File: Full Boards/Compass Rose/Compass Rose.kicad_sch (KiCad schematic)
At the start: 245 parts, among them J1 Program Header, J2 Future Bonding, Q10 2N3904, Q11 AO3401A, Q12 2N3904, Q7 AO3401A, Q8 2N3904, Q9 AO3401A, SW1 SW_MEC_5G, SW2 SW_MEC_5G, U1 ISO1044BD, U2 LM1117MP-5.0, U3 MAX3232, U4 STM32C092KCT6, U5 IS31FL3731-SA, U6 FM24CL64B-G, U7 FM24CL64B-G

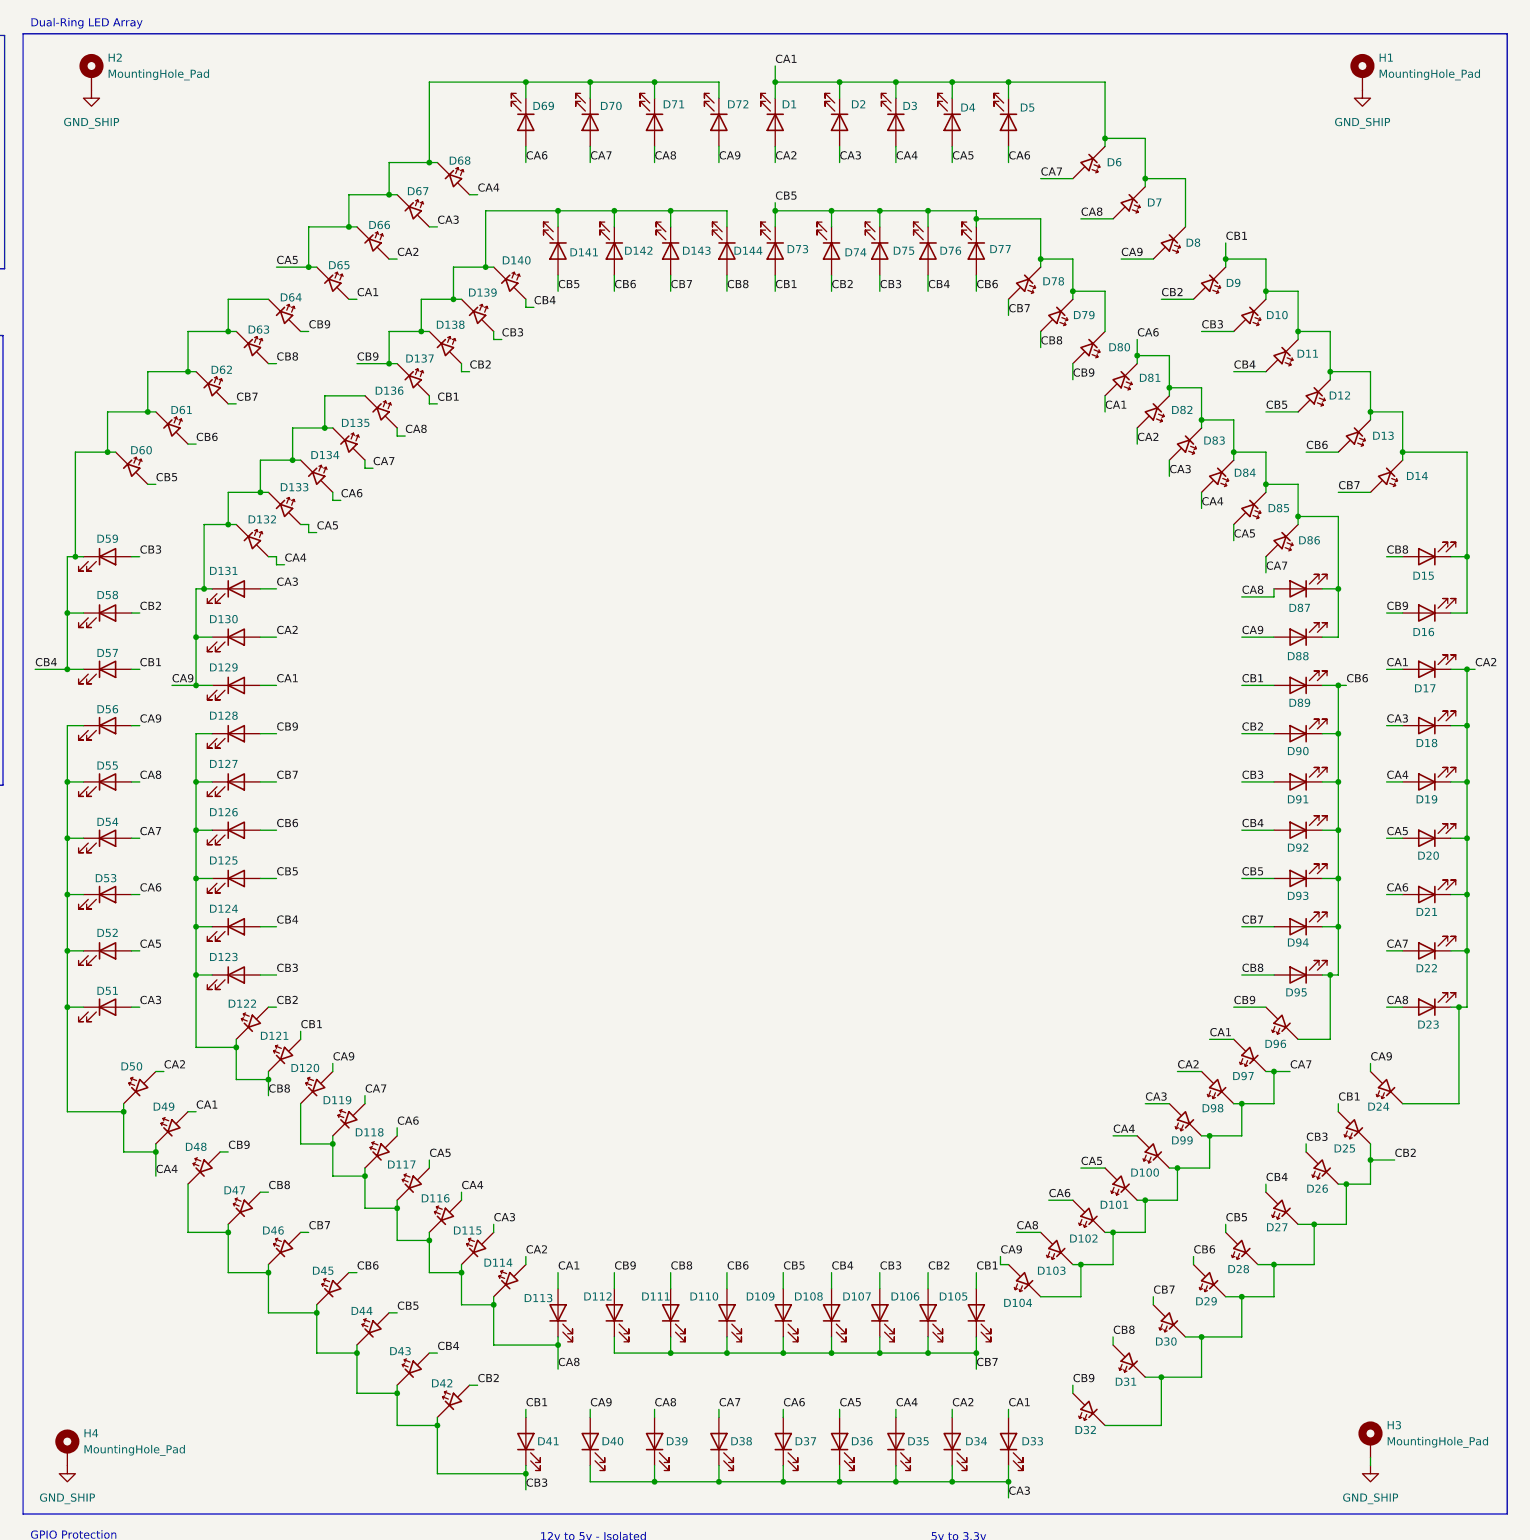
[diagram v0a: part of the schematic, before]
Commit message: Started updating the compass rose.
Signed-off-by: digimer <digital.mermaid@gmail.com>
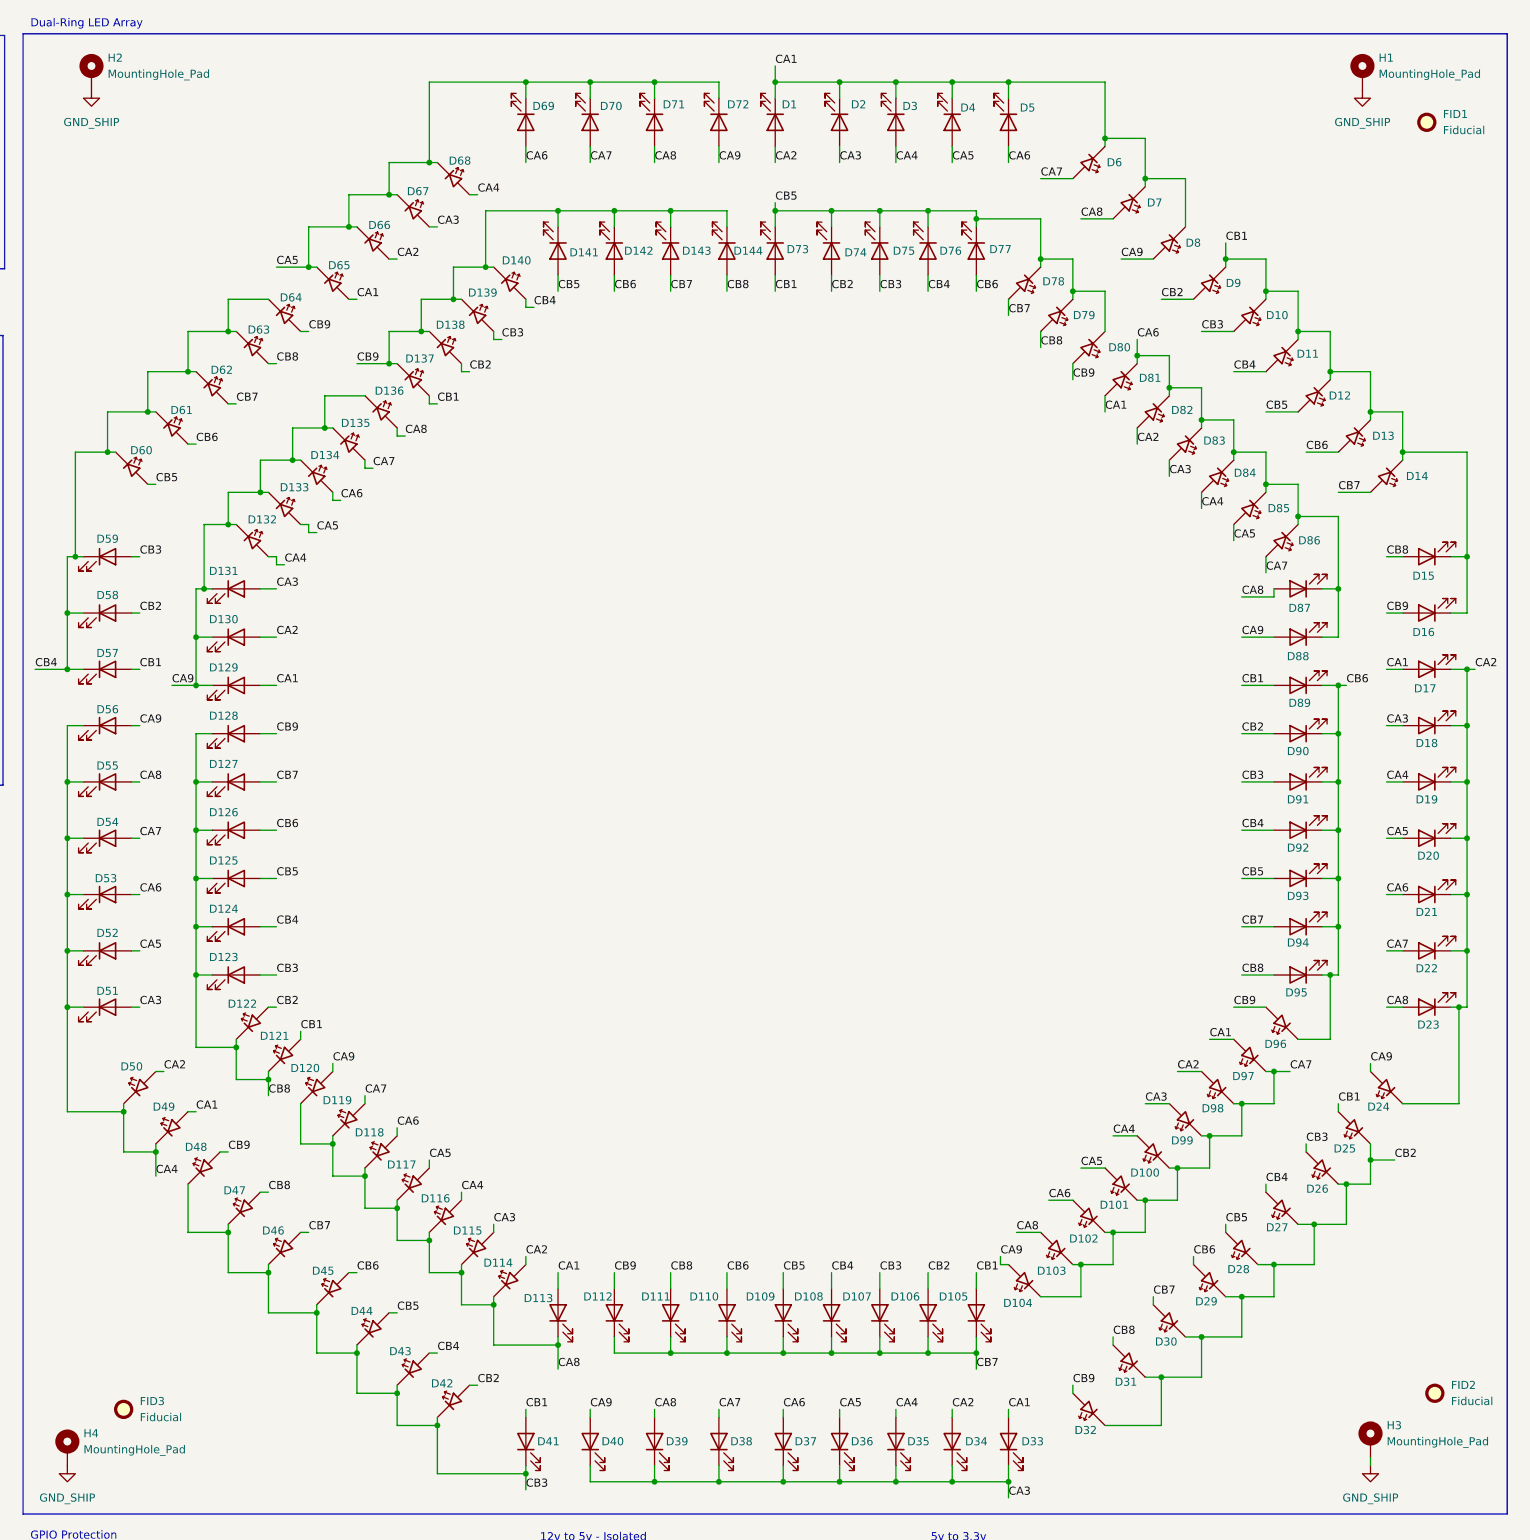
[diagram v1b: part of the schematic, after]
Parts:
- added FID1, FID2, FID3: Fiducial, symbol Mechanical:Fiducial
- DE1, DE2, LCD1, N2K1: value ~ -> (none)

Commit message: First update of the Compass Rose PCB.
Signed-off-by: digimer <digital.mermaid@gmail.com>
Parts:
- removed C6: TDK FA28NP01H152JNU06, mr-stuff:TDK CAPRB500W50L400T250H550, symbol mr-parts:TDK FA28NP01H152JNU06
- removed J2: Future Bonding, Connector_PinHeader_2.54mm:PinHeader_1x03_P2.54mm_Vertical, symbol Connector:Conn_01x03_Pin
- removed LR1: NCV8730ASN500T1G, mr-stuff:TSOP-5_483_OSI, symbol mr-parts:NCV8730ASN500T1G
- removed N2K1: (no value), mr-stuff:M12B-05PMMR, symbol mr-parts:M12B-05PMMR
- removed PS2: SPBW06F-05, mr-stuff:SPBW06F05, symbol mr-parts:SPBW06F-05
- removed SW1, SW2: SW_MEC_5G, mr-stuff:SW_TS03-66-50-BK-160-LCR-D-67, symbol Switch:SW_MEC_5G
- removed TP1: TP_VRAW, Connector_PinHeader_2.54mm:PinHeader_1x01_P2.54mm_Vertical, symbol Connector:Conn_01x01_Pin
- removed TP2, TP6: GND_SHIP, Connector_PinHeader_2.54mm:PinHeader_1x01_P2.54mm_Vertical, symbol Connector:Conn_01x01_Pin
- removed TP5: +5V_SHIP, Connector_PinHeader_2.54mm:PinHeader_1x01_P2.54mm_Vertical, symbol Connector:Conn_01x01_Pin
- removed U3: MAX3232, Package_SO:TSSOP-16_4.4x5mm_P0.65mm, symbol mr-parts:TI MAX3232EIPWRQ1
- added C6: 1500 pF, mr-stuff:TDK FA 5.0mm, symbol Device:C
- added IDCB1: SPBW06F-05, mr-stuff:Meanwell SPBW06F05, symbol mr-parts:Meanwell SPBW06F-05
- added J2: Opional Bond, Connector_PinHeader_2.54mm:PinHeader_1x02_P2.54mm_Vertical, symbol Connector:Conn_01x02_Pin
- added LVR1: NCV8730ASN500T1G, mr-stuff:Onsemi NCV8730, symbol mr-parts:Onsemi NCV8730ASN500T1G
- added RST1: MAX3232, mr-stuff:TI MAX3232EIPWRQ1, symbol mr-parts:TI MAX3232EIPWRQ1
- added SW1: Boot, mr-stuff:Same Sky TS03-66, symbol mr-parts:Same Sky TS03-66-50-BK-160-LCR-D-67
- added SW2: Reset, mr-stuff:Same Sky TS03-66, symbol mr-parts:Same Sky TS03-66-50-BK-160-LCR-D-67
- added TB1: 1862440, mr-stuff:Phoenix Contact 1862440, symbol mr-parts:Phoenix Contact 1862440
- added TP1: Iso Power, Connector_PinHeader_2.54mm:PinHeader_1x01_P2.54mm_Vertical, symbol Connector:Conn_01x02_Pin
- C14: footprint mr-stuff:RCER71E475K2A2H03B -> mr-stuff:Murata RCER71E
- D1: renamed from D145; Part (none) -> STM 1N5822RL
- DE1: value (none) -> L77SDE09SA4CH4F; symbol mr-parts:DE9_Socket -> mr-parts:Amphenol L77SDE09SA4CH4F; Part (none) -> Amphenol L77SDE09SA4CH4F
- ICT1: renamed from U1; value ISO1044BD -> TI_ISO1044BDR; symbol Interface_CAN_LIN:ISO1044BD -> mr-parts:TI_ISO1044BDR; Part (none) -> TI ISO1044BDR
- LCD1: value (none) -> 2x16 Char RGB I2C; footprint mr-stuff:NHD-0216K3Z-NS(RGB)-FBW-V3 -> mr-stuff:Newhaven Display NHD-0216K3Z-NS(RGB)-FBW-V3; symbol mr-parts:NHD-0216K3Z-FS(RGB)-FBW-V3 -> mr-parts:Newhaven Display NHD-0216K3Z-FS(RGB)-FBW-V3
- LED1: renamed from D1; value LED -> WP383SURDTK; footprint mr-stuff:WP383SURDTK -> mr-stuff:Kingbright WP383SURDTK; symbol Device:LED -> mr-parts:Kingbright WP383SURDTK; Part (none) -> Kingbright WP383SURDTK
- LED10: renamed from D10; value LED_45deg -> WP383SURDTK; footprint mr-stuff:WP383SURDTK -> mr-stuff:Kingbright WP383SURDTK; symbol Device:LED_45deg -> mr-parts:Kingbright_WP383SURDTK_45DEG; Part (none) -> Kingbright WP383SURDTK
- LED100: renamed from D100; value LED_45deg -> WP383SURDTK; footprint mr-stuff:WP383SURDTK -> mr-stuff:Kingbright WP383SURDTK; symbol Device:LED_45deg -> mr-parts:Kingbright_WP383SURDTK_45DEG; Part (none) -> Kingbright WP383SURDTK
- LED101: renamed from D101; value LED_45deg -> WP383SURDTK; footprint mr-stuff:WP383SURDTK -> mr-stuff:Kingbright WP383SURDTK; symbol Device:LED_45deg -> mr-parts:Kingbright_WP383SURDTK_45DEG; Part (none) -> Kingbright WP383SURDTK
- LED102: renamed from D102; value LED_45deg -> WP383SURDTK; footprint mr-stuff:WP383SURDTK -> mr-stuff:Kingbright WP383SURDTK; symbol Device:LED_45deg -> mr-parts:Kingbright_WP383SURDTK_45DEG; Part (none) -> Kingbright WP383SURDTK
- LED103: renamed from D103; value LED_45deg -> WP383SURDTK; footprint mr-stuff:WP383SURDTK -> mr-stuff:Kingbright WP383SURDTK; symbol Device:LED_45deg -> mr-parts:Kingbright_WP383SURDTK_45DEG; Part (none) -> Kingbright WP383SURDTK
- LED104: renamed from D104; value LED_45deg -> WP383SURDTK; footprint mr-stuff:WP383SURDTK -> mr-stuff:Kingbright WP383SURDTK; symbol Device:LED_45deg -> mr-parts:Kingbright_WP383SURDTK_45DEG; Part (none) -> Kingbright WP383SURDTK
- LED105: renamed from D105; value LED -> WP383SURDTK; footprint mr-stuff:WP383SURDTK -> mr-stuff:Kingbright WP383SURDTK; symbol Device:LED -> mr-parts:Kingbright WP383SURDTK; Part (none) -> Kingbright WP383SURDTK
- LED106: renamed from D106; value LED -> WP383SURDTK; footprint mr-stuff:WP383SURDTK -> mr-stuff:Kingbright WP383SURDTK; symbol Device:LED -> mr-parts:Kingbright WP383SURDTK; Part (none) -> Kingbright WP383SURDTK
- LED107: renamed from D107; value LED -> WP383SURDTK; footprint mr-stuff:WP383SURDTK -> mr-stuff:Kingbright WP383SURDTK; symbol Device:LED -> mr-parts:Kingbright WP383SURDTK; Part (none) -> Kingbright WP383SURDTK
- LED108: renamed from D108; value LED -> WP383SURDTK; footprint mr-stuff:WP383SURDTK -> mr-stuff:Kingbright WP383SURDTK; symbol Device:LED -> mr-parts:Kingbright WP383SURDTK; Part (none) -> Kingbright WP383SURDTK
- LED109: renamed from D109; value LED -> WP383SURDTK; footprint mr-stuff:WP383SURDTK -> mr-stuff:Kingbright WP383SURDTK; symbol Device:LED -> mr-parts:Kingbright WP383SURDTK; Part (none) -> Kingbright WP383SURDTK
- LED11: renamed from D11; value LED_45deg -> WP383SURDTK; footprint mr-stuff:WP383SURDTK -> mr-stuff:Kingbright WP383SURDTK; symbol Device:LED_45deg -> mr-parts:Kingbright_WP383SURDTK_45DEG; Part (none) -> Kingbright WP383SURDTK
- LED110: renamed from D110; value LED -> WP383SURDTK; footprint mr-stuff:WP383SURDTK -> mr-stuff:Kingbright WP383SURDTK; symbol Device:LED -> mr-parts:Kingbright WP383SURDTK; Part (none) -> Kingbright WP383SURDTK
- LED111: renamed from D111; value LED -> WP383SURDTK; footprint mr-stuff:WP383SURDTK -> mr-stuff:Kingbright WP383SURDTK; symbol Device:LED -> mr-parts:Kingbright WP383SURDTK; Part (none) -> Kingbright WP383SURDTK
- LED112: renamed from D112; value LED -> WP383SURDTK; footprint mr-stuff:WP383SURDTK -> mr-stuff:Kingbright WP383SURDTK; symbol Device:LED -> mr-parts:Kingbright WP383SURDTK; Part (none) -> Kingbright WP383SURDTK
- LED113: renamed from D113; value LED -> WP383SURDTK; footprint mr-stuff:WP383SURDTK -> mr-stuff:Kingbright WP383SURDTK; symbol Device:LED -> mr-parts:Kingbright WP383SURDTK; Part (none) -> Kingbright WP383SURDTK
- LED114: renamed from D114; value LED_45deg -> WP383SURDTK; footprint mr-stuff:WP383SURDTK -> mr-stuff:Kingbright WP383SURDTK; symbol Device:LED_45deg -> mr-parts:Kingbright_WP383SURDTK_45DEG; Part (none) -> Kingbright WP383SURDTK
- LED115: renamed from D115; value LED_45deg -> WP383SURDTK; footprint mr-stuff:WP383SURDTK -> mr-stuff:Kingbright WP383SURDTK; symbol Device:LED_45deg -> mr-parts:Kingbright_WP383SURDTK_45DEG; Part (none) -> Kingbright WP383SURDTK
- LED116: renamed from D116; value LED_45deg -> WP383SURDTK; footprint mr-stuff:WP383SURDTK -> mr-stuff:Kingbright WP383SURDTK; symbol Device:LED_45deg -> mr-parts:Kingbright_WP383SURDTK_45DEG; Part (none) -> Kingbright WP383SURDTK
- LED117: renamed from D117; value LED_45deg -> WP383SURDTK; footprint mr-stuff:WP383SURDTK -> mr-stuff:Kingbright WP383SURDTK; symbol Device:LED_45deg -> mr-parts:Kingbright_WP383SURDTK_45DEG; Part (none) -> Kingbright WP383SURDTK
- LED118: renamed from D118; value LED_45deg -> WP383SURDTK; footprint mr-stuff:WP383SURDTK -> mr-stuff:Kingbright WP383SURDTK; symbol Device:LED_45deg -> mr-parts:Kingbright_WP383SURDTK_45DEG; Part (none) -> Kingbright WP383SURDTK
- LED119: renamed from D119; value LED_45deg -> WP383SURDTK; footprint mr-stuff:WP383SURDTK -> mr-stuff:Kingbright WP383SURDTK; symbol Device:LED_45deg -> mr-parts:Kingbright_WP383SURDTK_45DEG; Part (none) -> Kingbright WP383SURDTK
- LED12: renamed from D12; value LED_45deg -> WP383SURDTK; footprint mr-stuff:WP383SURDTK -> mr-stuff:Kingbright WP383SURDTK; symbol Device:LED_45deg -> mr-parts:Kingbright_WP383SURDTK_45DEG; Part (none) -> Kingbright WP383SURDTK
- LED120: renamed from D120; value LED_45deg -> WP383SURDTK; footprint mr-stuff:WP383SURDTK -> mr-stuff:Kingbright WP383SURDTK; symbol Device:LED_45deg -> mr-parts:Kingbright_WP383SURDTK_45DEG; Part (none) -> Kingbright WP383SURDTK
- LED121: renamed from D121; value LED_45deg -> WP383SURDTK; footprint mr-stuff:WP383SURDTK -> mr-stuff:Kingbright WP383SURDTK; symbol Device:LED_45deg -> mr-parts:Kingbright_WP383SURDTK_45DEG; Part (none) -> Kingbright WP383SURDTK
- LED122: renamed from D122; value LED_45deg -> WP383SURDTK; footprint mr-stuff:WP383SURDTK -> mr-stuff:Kingbright WP383SURDTK; symbol Device:LED_45deg -> mr-parts:Kingbright_WP383SURDTK_45DEG; Part (none) -> Kingbright WP383SURDTK
- LED123: renamed from D123; value LED -> WP383SURDTK; footprint mr-stuff:WP383SURDTK -> mr-stuff:Kingbright WP383SURDTK; symbol Device:LED -> mr-parts:Kingbright WP383SURDTK; Part (none) -> Kingbright WP383SURDTK
- LED124: renamed from D124; value LED -> WP383SURDTK; footprint mr-stuff:WP383SURDTK -> mr-stuff:Kingbright WP383SURDTK; symbol Device:LED -> mr-parts:Kingbright WP383SURDTK; Part (none) -> Kingbright WP383SURDTK
- LED125: renamed from D125; value LED -> WP383SURDTK; footprint mr-stuff:WP383SURDTK -> mr-stuff:Kingbright WP383SURDTK; symbol Device:LED -> mr-parts:Kingbright WP383SURDTK; Part (none) -> Kingbright WP383SURDTK
- LED126: renamed from D126; value LED -> WP383SURDTK; footprint mr-stuff:WP383SURDTK -> mr-stuff:Kingbright WP383SURDTK; symbol Device:LED -> mr-parts:Kingbright WP383SURDTK; Part (none) -> Kingbright WP383SURDTK
- LED127: renamed from D127; value LED -> WP383SURDTK; footprint mr-stuff:WP383SURDTK -> mr-stuff:Kingbright WP383SURDTK; symbol Device:LED -> mr-parts:Kingbright WP383SURDTK; Part (none) -> Kingbright WP383SURDTK
- LED128: renamed from D128; value LED -> WP383SURDTK; footprint mr-stuff:WP383SURDTK -> mr-stuff:Kingbright WP383SURDTK; symbol Device:LED -> mr-parts:Kingbright WP383SURDTK; Part (none) -> Kingbright WP383SURDTK
- LED129: renamed from D129; value LED -> WP383SURDTK; footprint mr-stuff:WP383SURDTK -> mr-stuff:Kingbright WP383SURDTK; symbol Device:LED -> mr-parts:Kingbright WP383SURDTK; Part (none) -> Kingbright WP383SURDTK
- LED13: renamed from D13; value LED_45deg -> WP383SURDTK; footprint mr-stuff:WP383SURDTK -> mr-stuff:Kingbright WP383SURDTK; symbol Device:LED_45deg -> mr-parts:Kingbright_WP383SURDTK_45DEG; Part (none) -> Kingbright WP383SURDTK
- LED130: renamed from D130; value LED -> WP383SURDTK; footprint mr-stuff:WP383SURDTK -> mr-stuff:Kingbright WP383SURDTK; symbol Device:LED -> mr-parts:Kingbright WP383SURDTK; Part (none) -> Kingbright WP383SURDTK
- LED131: renamed from D131; value LED -> WP383SURDTK; footprint mr-stuff:WP383SURDTK -> mr-stuff:Kingbright WP383SURDTK; symbol Device:LED -> mr-parts:Kingbright WP383SURDTK; Part (none) -> Kingbright WP383SURDTK
- LED132: renamed from D132; value LED_45deg -> WP383SURDTK; footprint mr-stuff:WP383SURDTK -> mr-stuff:Kingbright WP383SURDTK; symbol Device:LED_45deg -> mr-parts:Kingbright_WP383SURDTK_45DEG; Part (none) -> Kingbright WP383SURDTK
- LED133: renamed from D133; value LED_45deg -> WP383SURDTK; footprint mr-stuff:WP383SURDTK -> mr-stuff:Kingbright WP383SURDTK; symbol Device:LED_45deg -> mr-parts:Kingbright_WP383SURDTK_45DEG; Part (none) -> Kingbright WP383SURDTK
- LED134: renamed from D134; value LED_45deg -> WP383SURDTK; footprint mr-stuff:WP383SURDTK -> mr-stuff:Kingbright WP383SURDTK; symbol Device:LED_45deg -> mr-parts:Kingbright_WP383SURDTK_45DEG; Part (none) -> Kingbright WP383SURDTK
- LED135: renamed from D135; value LED_45deg -> WP383SURDTK; footprint mr-stuff:WP383SURDTK -> mr-stuff:Kingbright WP383SURDTK; symbol Device:LED_45deg -> mr-parts:Kingbright_WP383SURDTK_45DEG; Part (none) -> Kingbright WP383SURDTK
- LED136: renamed from D136; value LED_45deg -> WP383SURDTK; footprint mr-stuff:WP383SURDTK -> mr-stuff:Kingbright WP383SURDTK; symbol Device:LED_45deg -> mr-parts:Kingbright_WP383SURDTK_45DEG; Part (none) -> Kingbright WP383SURDTK
- LED137: renamed from D137; value LED_45deg -> WP383SURDTK; footprint mr-stuff:WP383SURDTK -> mr-stuff:Kingbright WP383SURDTK; symbol Device:LED_45deg -> mr-parts:Kingbright_WP383SURDTK_45DEG; Part (none) -> Kingbright WP383SURDTK
- LED138: renamed from D138; value LED_45deg -> WP383SURDTK; footprint mr-stuff:WP383SURDTK -> mr-stuff:Kingbright WP383SURDTK; symbol Device:LED_45deg -> mr-parts:Kingbright_WP383SURDTK_45DEG; Part (none) -> Kingbright WP383SURDTK
- LED139: renamed from D139; value LED_45deg -> WP383SURDTK; footprint mr-stuff:WP383SURDTK -> mr-stuff:Kingbright WP383SURDTK; symbol Device:LED_45deg -> mr-parts:Kingbright_WP383SURDTK_45DEG; Part (none) -> Kingbright WP383SURDTK
- LED14: renamed from D14; value LED_45deg -> WP383SURDTK; footprint mr-stuff:WP383SURDTK -> mr-stuff:Kingbright WP383SURDTK; symbol Device:LED_45deg -> mr-parts:Kingbright_WP383SURDTK_45DEG; Part (none) -> Kingbright WP383SURDTK
- LED140: renamed from D140; value LED_45deg -> WP383SURDTK; footprint mr-stuff:WP383SURDTK -> mr-stuff:Kingbright WP383SURDTK; symbol Device:LED_45deg -> mr-parts:Kingbright_WP383SURDTK_45DEG; Part (none) -> Kingbright WP383SURDTK
- LED141: renamed from D141; value LED -> WP383SURDTK; footprint mr-stuff:WP383SURDTK -> mr-stuff:Kingbright WP383SURDTK; symbol Device:LED -> mr-parts:Kingbright WP383SURDTK; Part (none) -> Kingbright WP383SURDTK
- LED142: renamed from D142; value LED -> WP383SURDTK; footprint mr-stuff:WP383SURDTK -> mr-stuff:Kingbright WP383SURDTK; symbol Device:LED -> mr-parts:Kingbright WP383SURDTK; Part (none) -> Kingbright WP383SURDTK
- LED143: renamed from D143; value LED -> WP383SURDTK; footprint mr-stuff:WP383SURDTK -> mr-stuff:Kingbright WP383SURDTK; symbol Device:LED -> mr-parts:Kingbright WP383SURDTK; Part (none) -> Kingbright WP383SURDTK
- LED144: renamed from D144; value LED -> WP383SURDTK; footprint mr-stuff:WP383SURDTK -> mr-stuff:Kingbright WP383SURDTK; symbol Device:LED -> mr-parts:Kingbright WP383SURDTK; Part (none) -> Kingbright WP383SURDTK
- LED15: renamed from D15; value LED -> WP383SURDTK; footprint mr-stuff:WP383SURDTK -> mr-stuff:Kingbright WP383SURDTK; symbol Device:LED -> mr-parts:Kingbright WP383SURDTK; Part (none) -> Kingbright WP383SURDTK
- LED16: renamed from D16; value LED -> WP383SURDTK; footprint mr-stuff:WP383SURDTK -> mr-stuff:Kingbright WP383SURDTK; symbol Device:LED -> mr-parts:Kingbright WP383SURDTK; Part (none) -> Kingbright WP383SURDTK
- LED17: renamed from D17; value LED -> WP383SURDTK; footprint mr-stuff:WP383SURDTK -> mr-stuff:Kingbright WP383SURDTK; symbol Device:LED -> mr-parts:Kingbright WP383SURDTK; Part (none) -> Kingbright WP383SURDTK
- LED18: renamed from D18; value LED -> WP383SURDTK; footprint mr-stuff:WP383SURDTK -> mr-stuff:Kingbright WP383SURDTK; symbol Device:LED -> mr-parts:Kingbright WP383SURDTK; Part (none) -> Kingbright WP383SURDTK
- LED19: renamed from D19; value LED -> WP383SURDTK; footprint mr-stuff:WP383SURDTK -> mr-stuff:Kingbright WP383SURDTK; symbol Device:LED -> mr-parts:Kingbright WP383SURDTK; Part (none) -> Kingbright WP383SURDTK
- LED2: renamed from D2; value LED -> WP383SURDTK; footprint mr-stuff:WP383SURDTK -> mr-stuff:Kingbright WP383SURDTK; symbol Device:LED -> mr-parts:Kingbright WP383SURDTK; Part (none) -> Kingbright WP383SURDTK
- LED20: renamed from D20; value LED -> WP383SURDTK; footprint mr-stuff:WP383SURDTK -> mr-stuff:Kingbright WP383SURDTK; symbol Device:LED -> mr-parts:Kingbright WP383SURDTK; Part (none) -> Kingbright WP383SURDTK
- LED21: renamed from D21; value LED -> WP383SURDTK; footprint mr-stuff:WP383SURDTK -> mr-stuff:Kingbright WP383SURDTK; symbol Device:LED -> mr-parts:Kingbright WP383SURDTK; Part (none) -> Kingbright WP383SURDTK
- LED22: renamed from D22; value LED -> WP383SURDTK; footprint mr-stuff:WP383SURDTK -> mr-stuff:Kingbright WP383SURDTK; symbol Device:LED -> mr-parts:Kingbright WP383SURDTK; Part (none) -> Kingbright WP383SURDTK
- LED23: renamed from D23; value LED -> WP383SURDTK; footprint mr-stuff:WP383SURDTK -> mr-stuff:Kingbright WP383SURDTK; symbol Device:LED -> mr-parts:Kingbright WP383SURDTK; Part (none) -> Kingbright WP383SURDTK
- LED24: renamed from D24; value LED_45deg -> WP383SURDTK; footprint mr-stuff:WP383SURDTK -> mr-stuff:Kingbright WP383SURDTK; symbol Device:LED_45deg -> mr-parts:Kingbright_WP383SURDTK_45DEG; Part (none) -> Kingbright WP383SURDTK
- LED25: renamed from D25; value LED_45deg -> WP383SURDTK; footprint mr-stuff:WP383SURDTK -> mr-stuff:Kingbright WP383SURDTK; symbol Device:LED_45deg -> mr-parts:Kingbright_WP383SURDTK_45DEG; Part (none) -> Kingbright WP383SURDTK
- LED26: renamed from D26; value LED_45deg -> WP383SURDTK; footprint mr-stuff:WP383SURDTK -> mr-stuff:Kingbright WP383SURDTK; symbol Device:LED_45deg -> mr-parts:Kingbright_WP383SURDTK_45DEG; Part (none) -> Kingbright WP383SURDTK
- LED27: renamed from D27; value LED_45deg -> WP383SURDTK; footprint mr-stuff:WP383SURDTK -> mr-stuff:Kingbright WP383SURDTK; symbol Device:LED_45deg -> mr-parts:Kingbright_WP383SURDTK_45DEG; Part (none) -> Kingbright WP383SURDTK
- LED28: renamed from D28; value LED_45deg -> WP383SURDTK; footprint mr-stuff:WP383SURDTK -> mr-stuff:Kingbright WP383SURDTK; symbol Device:LED_45deg -> mr-parts:Kingbright_WP383SURDTK_45DEG; Part (none) -> Kingbright WP383SURDTK
- LED29: renamed from D29; value LED_45deg -> WP383SURDTK; footprint mr-stuff:WP383SURDTK -> mr-stuff:Kingbright WP383SURDTK; symbol Device:LED_45deg -> mr-parts:Kingbright_WP383SURDTK_45DEG; Part (none) -> Kingbright WP383SURDTK
- LED3: renamed from D3; value LED -> WP383SURDTK; footprint mr-stuff:WP383SURDTK -> mr-stuff:Kingbright WP383SURDTK; symbol Device:LED -> mr-parts:Kingbright WP383SURDTK; Part (none) -> Kingbright WP383SURDTK
- LED30: renamed from D30; value LED_45deg -> WP383SURDTK; footprint mr-stuff:WP383SURDTK -> mr-stuff:Kingbright WP383SURDTK; symbol Device:LED_45deg -> mr-parts:Kingbright_WP383SURDTK_45DEG; Part (none) -> Kingbright WP383SURDTK
- LED31: renamed from D31; value LED_45deg -> WP383SURDTK; footprint mr-stuff:WP383SURDTK -> mr-stuff:Kingbright WP383SURDTK; symbol Device:LED_45deg -> mr-parts:Kingbright_WP383SURDTK_45DEG; Part (none) -> Kingbright WP383SURDTK
- LED32: renamed from D32; value LED_45deg -> WP383SURDTK; footprint mr-stuff:WP383SURDTK -> mr-stuff:Kingbright WP383SURDTK; symbol Device:LED_45deg -> mr-parts:Kingbright_WP383SURDTK_45DEG; Part (none) -> Kingbright WP383SURDTK
- LED33: renamed from D33; value LED -> WP383SURDTK; footprint mr-stuff:WP383SURDTK -> mr-stuff:Kingbright WP383SURDTK; symbol Device:LED -> mr-parts:Kingbright WP383SURDTK; Part (none) -> Kingbright WP383SURDTK
- LED34: renamed from D34; value LED -> WP383SURDTK; footprint mr-stuff:WP383SURDTK -> mr-stuff:Kingbright WP383SURDTK; symbol Device:LED -> mr-parts:Kingbright WP383SURDTK; Part (none) -> Kingbright WP383SURDTK
- LED35: renamed from D35; value LED -> WP383SURDTK; footprint mr-stuff:WP383SURDTK -> mr-stuff:Kingbright WP383SURDTK; symbol Device:LED -> mr-parts:Kingbright WP383SURDTK; Part (none) -> Kingbright WP383SURDTK
- LED36: renamed from D36; value LED -> WP383SURDTK; footprint mr-stuff:WP383SURDTK -> mr-stuff:Kingbright WP383SURDTK; symbol Device:LED -> mr-parts:Kingbright WP383SURDTK; Part (none) -> Kingbright WP383SURDTK
- LED37: renamed from D37; value LED -> WP383SURDTK; footprint mr-stuff:WP383SURDTK -> mr-stuff:Kingbright WP383SURDTK; symbol Device:LED -> mr-parts:Kingbright WP383SURDTK; Part (none) -> Kingbright WP383SURDTK
- LED38: renamed from D38; value LED -> WP383SURDTK; footprint mr-stuff:WP383SURDTK -> mr-stuff:Kingbright WP383SURDTK; symbol Device:LED -> mr-parts:Kingbright WP383SURDTK; Part (none) -> Kingbright WP383SURDTK
- LED39: renamed from D39; value LED -> WP383SURDTK; footprint mr-stuff:WP383SURDTK -> mr-stuff:Kingbright WP383SURDTK; symbol Device:LED -> mr-parts:Kingbright WP383SURDTK; Part (none) -> Kingbright WP383SURDTK
- LED4: renamed from D4; value LED -> WP383SURDTK; footprint mr-stuff:WP383SURDTK -> mr-stuff:Kingbright WP383SURDTK; symbol Device:LED -> mr-parts:Kingbright WP383SURDTK; Part (none) -> Kingbright WP383SURDTK
- LED40: renamed from D40; value LED -> WP383SURDTK; footprint mr-stuff:WP383SURDTK -> mr-stuff:Kingbright WP383SURDTK; symbol Device:LED -> mr-parts:Kingbright WP383SURDTK; Part (none) -> Kingbright WP383SURDTK
- LED41: renamed from D41; value LED -> WP383SURDTK; footprint mr-stuff:WP383SURDTK -> mr-stuff:Kingbright WP383SURDTK; symbol Device:LED -> mr-parts:Kingbright WP383SURDTK; Part (none) -> Kingbright WP383SURDTK
- LED42: renamed from D42; value LED_45deg -> WP383SURDTK; footprint mr-stuff:WP383SURDTK -> mr-stuff:Kingbright WP383SURDTK; symbol Device:LED_45deg -> mr-parts:Kingbright_WP383SURDTK_45DEG; Part (none) -> Kingbright WP383SURDTK
- LED43: renamed from D43; value LED_45deg -> WP383SURDTK; footprint mr-stuff:WP383SURDTK -> mr-stuff:Kingbright WP383SURDTK; symbol Device:LED_45deg -> mr-parts:Kingbright_WP383SURDTK_45DEG; Part (none) -> Kingbright WP383SURDTK
- LED44: renamed from D44; value LED_45deg -> WP383SURDTK; footprint mr-stuff:WP383SURDTK -> mr-stuff:Kingbright WP383SURDTK; symbol Device:LED_45deg -> mr-parts:Kingbright_WP383SURDTK_45DEG; Part (none) -> Kingbright WP383SURDTK
- LED45: renamed from D45; value LED_45deg -> WP383SURDTK; footprint mr-stuff:WP383SURDTK -> mr-stuff:Kingbright WP383SURDTK; symbol Device:LED_45deg -> mr-parts:Kingbright_WP383SURDTK_45DEG; Part (none) -> Kingbright WP383SURDTK
- LED46: renamed from D46; value LED_45deg -> WP383SURDTK; footprint mr-stuff:WP383SURDTK -> mr-stuff:Kingbright WP383SURDTK; symbol Device:LED_45deg -> mr-parts:Kingbright_WP383SURDTK_45DEG; Part (none) -> Kingbright WP383SURDTK
- LED47: renamed from D47; value LED_45deg -> WP383SURDTK; footprint mr-stuff:WP383SURDTK -> mr-stuff:Kingbright WP383SURDTK; symbol Device:LED_45deg -> mr-parts:Kingbright_WP383SURDTK_45DEG; Part (none) -> Kingbright WP383SURDTK
- LED48: renamed from D48; value LED_45deg -> WP383SURDTK; footprint mr-stuff:WP383SURDTK -> mr-stuff:Kingbright WP383SURDTK; symbol Device:LED_45deg -> mr-parts:Kingbright_WP383SURDTK_45DEG; Part (none) -> Kingbright WP383SURDTK
- LED49: renamed from D49; value LED_45deg -> WP383SURDTK; footprint mr-stuff:WP383SURDTK -> mr-stuff:Kingbright WP383SURDTK; symbol Device:LED_45deg -> mr-parts:Kingbright_WP383SURDTK_45DEG; Part (none) -> Kingbright WP383SURDTK
- LED5: renamed from D5; value LED -> WP383SURDTK; footprint mr-stuff:WP383SURDTK -> mr-stuff:Kingbright WP383SURDTK; symbol Device:LED -> mr-parts:Kingbright WP383SURDTK; Part (none) -> Kingbright WP383SURDTK
- LED50: renamed from D50; value LED_45deg -> WP383SURDTK; footprint mr-stuff:WP383SURDTK -> mr-stuff:Kingbright WP383SURDTK; symbol Device:LED_45deg -> mr-parts:Kingbright_WP383SURDTK_45DEG; Part (none) -> Kingbright WP383SURDTK
- LED51: renamed from D51; value LED -> WP383SURDTK; footprint mr-stuff:WP383SURDTK -> mr-stuff:Kingbright WP383SURDTK; symbol Device:LED -> mr-parts:Kingbright WP383SURDTK; Part (none) -> Kingbright WP383SURDTK
- LED52: renamed from D52; value LED -> WP383SURDTK; footprint mr-stuff:WP383SURDTK -> mr-stuff:Kingbright WP383SURDTK; symbol Device:LED -> mr-parts:Kingbright WP383SURDTK; Part (none) -> Kingbright WP383SURDTK
- LED53: renamed from D53; value LED -> WP383SURDTK; footprint mr-stuff:WP383SURDTK -> mr-stuff:Kingbright WP383SURDTK; symbol Device:LED -> mr-parts:Kingbright WP383SURDTK; Part (none) -> Kingbright WP383SURDTK
- LED54: renamed from D54; value LED -> WP383SURDTK; footprint mr-stuff:WP383SURDTK -> mr-stuff:Kingbright WP383SURDTK; symbol Device:LED -> mr-parts:Kingbright WP383SURDTK; Part (none) -> Kingbright WP383SURDTK
- LED55: renamed from D55; value LED -> WP383SURDTK; footprint mr-stuff:WP383SURDTK -> mr-stuff:Kingbright WP383SURDTK; symbol Device:LED -> mr-parts:Kingbright WP383SURDTK; Part (none) -> Kingbright WP383SURDTK
- LED56: renamed from D56; value LED -> WP383SURDTK; footprint mr-stuff:WP383SURDTK -> mr-stuff:Kingbright WP383SURDTK; symbol Device:LED -> mr-parts:Kingbright WP383SURDTK; Part (none) -> Kingbright WP383SURDTK
- LED57: renamed from D57; value LED -> WP383SURDTK; footprint mr-stuff:WP383SURDTK -> mr-stuff:Kingbright WP383SURDTK; symbol Device:LED -> mr-parts:Kingbright WP383SURDTK; Part (none) -> Kingbright WP383SURDTK
- LED58: renamed from D58; value LED -> WP383SURDTK; footprint mr-stuff:WP383SURDTK -> mr-stuff:Kingbright WP383SURDTK; symbol Device:LED -> mr-parts:Kingbright WP383SURDTK; Part (none) -> Kingbright WP383SURDTK
- LED59: renamed from D59; value LED -> WP383SURDTK; footprint mr-stuff:WP383SURDTK -> mr-stuff:Kingbright WP383SURDTK; symbol Device:LED -> mr-parts:Kingbright WP383SURDTK; Part (none) -> Kingbright WP383SURDTK
- LED6: renamed from D6; value LED_45deg -> WP383SURDTK; footprint mr-stuff:WP383SURDTK -> mr-stuff:Kingbright WP383SURDTK; symbol Device:LED_45deg -> mr-parts:Kingbright_WP383SURDTK_45DEG; Part (none) -> Kingbright WP383SURDTK
- LED60: renamed from D60; value LED_45deg -> WP383SURDTK; footprint mr-stuff:WP383SURDTK -> mr-stuff:Kingbright WP383SURDTK; symbol Device:LED_45deg -> mr-parts:Kingbright_WP383SURDTK_45DEG; Part (none) -> Kingbright WP383SURDTK
- LED61: renamed from D61; value LED_45deg -> WP383SURDTK; footprint mr-stuff:WP383SURDTK -> mr-stuff:Kingbright WP383SURDTK; symbol Device:LED_45deg -> mr-parts:Kingbright_WP383SURDTK_45DEG; Part (none) -> Kingbright WP383SURDTK
- LED62: renamed from D62; value LED_45deg -> WP383SURDTK; footprint mr-stuff:WP383SURDTK -> mr-stuff:Kingbright WP383SURDTK; symbol Device:LED_45deg -> mr-parts:Kingbright_WP383SURDTK_45DEG; Part (none) -> Kingbright WP383SURDTK
- LED63: renamed from D63; value LED_45deg -> WP383SURDTK; footprint mr-stuff:WP383SURDTK -> mr-stuff:Kingbright WP383SURDTK; symbol Device:LED_45deg -> mr-parts:Kingbright_WP383SURDTK_45DEG; Part (none) -> Kingbright WP383SURDTK
- renumbered TVS1 to TVS2, TVS2 to TVS3, TVS3 to TVS4
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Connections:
- net +3.3V: now also RST1.10 (T2IN), RST1.16 (VCC), SW1.1 (A), SW1.2 (A)
- net +5V: now also C6.2, IDCB1.6 (+VOUT)
- net +5V_SHIP: now also LVR1.5 (OUT), TP1.2 (Pin_2)
- net DEBUG_SWCLK: now also SW1.3 (B), SW1.4 (B)
- net GND: now also C13.1, IDCB1.7 (-VOUT), RST1.15 (GND), SW2.3 (B), SW2.4 (B); no longer C13.2
- net GND_SHIP: now also IDCB1.1 (-VIN), J2.2 (Pin_2), LVR1.2 (GND), TB1.5, TB1.6, TP1.1 (Pin_1)
- net NRST: now also SW2.1 (A), SW2.2 (A)
- net USART1_RX: now also RST1.12 (R1OUT)
- net USART1_TX: now also RST1.11 (T1IN)
- net V_RAW: now also LVR1.1 (IN), LVR1.3 (EN)
- net at L1.2: now also C6.1, IDCB1.2 (+VIN)
- net at PTC1.2: now also TB1.3, TB1.4
- net at C10.1: now also RST1.1 (C1+)
- net at C10.2: now also RST1.3 (C1-)
- net at ICT1.5 (CANL): now also TB1.10, TB1.9
- net at ICT1.6 (CANH): now also TB1.7, TB1.8
- net at C11.1: now also RST1.4 (C2+)
- net at C11.2: now also RST1.5 (C2-)
- net RS232_RX: now reaches DE1.3
- net RS232_RX: now also RST1.13 (R1IN)
- net RS232_TX: now reaches DE1.4
- net RS232_TX: now also RST1.14 (T1OUT)
- net at C12.2: now also RST1.2 (VS+)
- new net: C13.2, RST1.6 (VS-)
- new net: J2.1 (Pin_1), TB1.1, TB1.2
- no-connect marks 29 -> 27
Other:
- note added: "TB1 Pins: 1. Shield 2. V_RAW 3. GND_SHIP 4. CAN High 5. CAN Low"
- note removed: "1500pF"
- note removed: "Boot"
- note removed: "Reset"
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
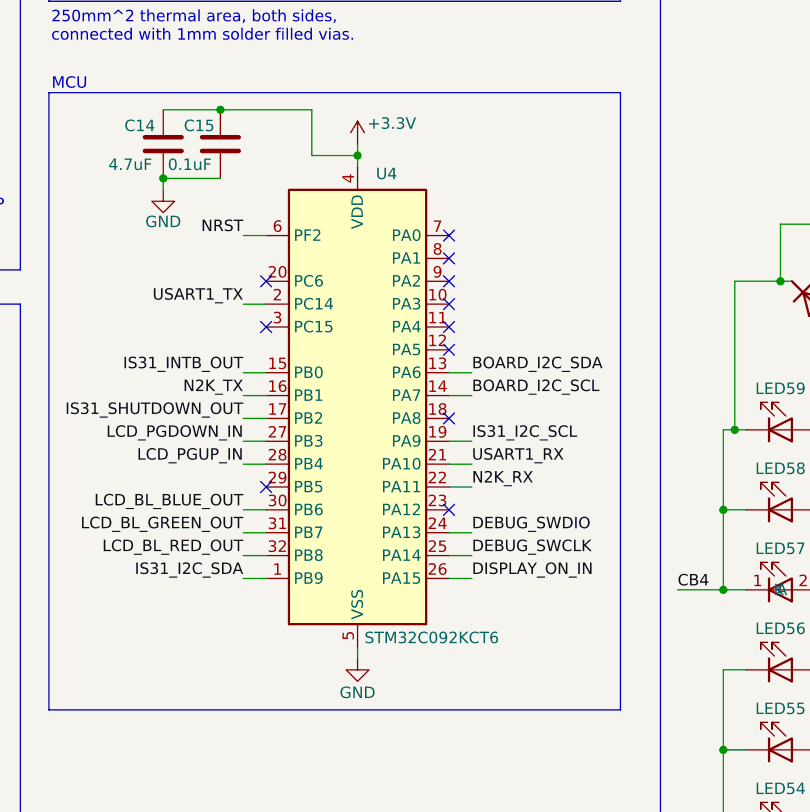
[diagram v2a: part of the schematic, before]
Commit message: Created a proper footprint and symbol for the STM32C092KCT6 to resolve the symbol name's package not matching the used footprint.
Signed-off-by: digimer <digital.mermaid@gmail.com>
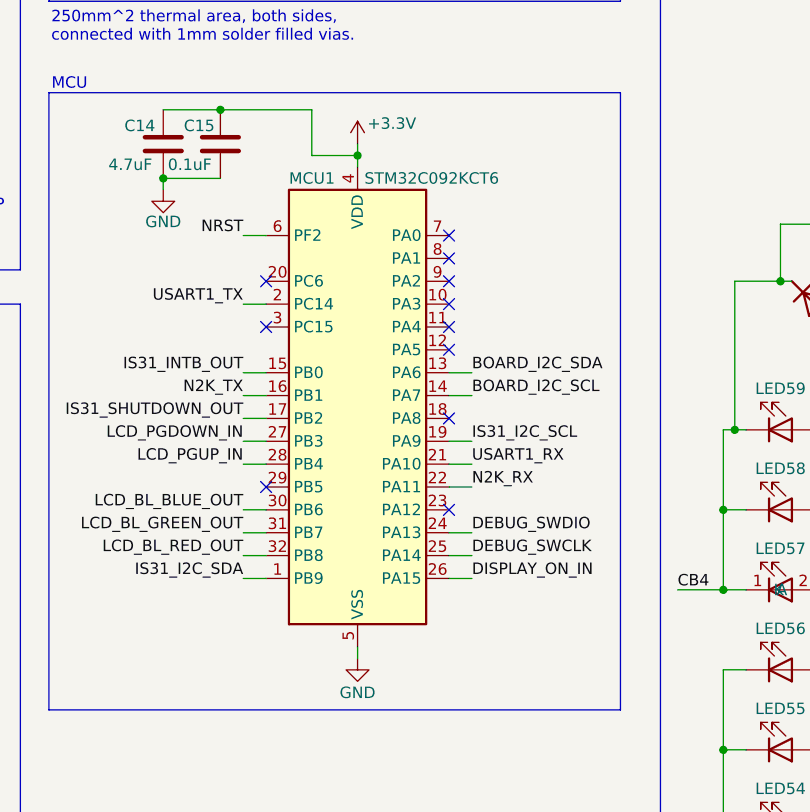
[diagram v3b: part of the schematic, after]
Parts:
- MCU1: renamed from U4; footprint Package_DFN_QFN:QFN-32-1EP_5x5mm_P0.5mm_EP3.45x3.45mm -> mr-stuff:STM STM32C0 LQFP-32; symbol MCU_ST_STM32C0:STM32C071KBUx -> mr-parts:STM STM32C092KCT6; Part (none) -> STM STM32C092KCT6
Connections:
- net GND: no longer MCU1.33 (VSS)
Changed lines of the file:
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@@
 	)
 	(symbol
-		(lib_id "MCU_ST_STM32C0:STM32C071KBUx")
+		(lib_id "mr-parts:STM STM32C092KCT6")
 		(at 135.89 99.06 0)
 		(unit 1)
@@
 		(in_pos_files yes)
 		(dnp no)
-		(property "Reference" "U4"
-			(at 137.922 71.882 0)
+		(property "Reference" "MCU1"
+			(at 128.27 72.39 0)
 			(show_name no)
 			(do_not_autoplace no)
@@
 		)
 		(property "Value" "STM32C092KCT6"
-			(at 136.652 123.444 0)
+			(at 136.652 72.39 0)
 			(show_name no)
 			(do_not_autoplace no)
@@
 			)
 		)
-		(property "Footprint" "Package_DFN_QFN:QFN-32-1EP_5x5mm_P0.5mm_EP3.45x3.45mm"
-			(at 128.27 121.92 0)
-			(hide yes)
-			(show_name no)
-			(do_not_autoplace no)
-			(effects
-				(font
-					(size 1.27 1.27)
-				)
-				(justify right)
-			)
-		)
-		(property "Datasheet" "https://www.st.com/resource/en/datasheet/stm32c071kb.pdf"
-			(at 135.89 99.06 0)
+		(property "Footprint" "mr-stuff:STM STM32C0 LQFP-32"
+			(at 135.89 143.002 0)
 			(hide yes)
 			(show_name no)
@@
 			)
 		)
-		(property "Description" "STMicroelectronics Arm Cortex-M0+ MCU, 128KB flash, 24KB RAM, 30 GPIO, UFQFPN32_GP"
-			(at 135.89 99.06 0)
+		(property "Datasheet" "https://www.st.com/resource/en/datasheet/stm32c091cb.pdf"
+			(at 136.144 137.922 0)
+			(hide yes)
+			(show_name no)
+			(do_not_autoplace no)
+			(effects
+				(font
+					(size 1.27 1.27)
+				)
+			)
+		)
+		(property "Description" "ARM® Cortex®-M0+ STM32C0 Microcontroller IC 32-Bit 48MHz 256KB (256K x 8) FLASH 32-LQFP (7x7)"
+			(at 135.89 140.462 0)
+			(hide yes)
+			(show_name no)
+			(do_not_autoplace no)
+			(effects
+				(font
+					(size 1.27 1.27)
+				)
+			)
+		)
+		(property "Part" "STM STM32C092KCT6"
+			(at 135.89 135.636 0)
 			(hide yes)
 			(show_name no)
@@
 		(pin "28"
 		)
-		(pin "33"
-		)
 		(pin "5"
 		)
@@
 			(project "Compass Rose"
 				(path "/e4671408-3e04-42c4-aa2c-7576ad4f645e"
-					(reference "U4")
+					(reference "MCU1")
 					(unit 1)
 				)
